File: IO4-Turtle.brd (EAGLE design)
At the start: 50 x 68.6 mm, 30 parts, among them CON1 RJ12/6, IC1 TC4428A, IC2 NE555S, Q1 NPN, X2 MSTBA5

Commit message: added values for connectors
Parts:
- J1: value (none) -> 0.156
- LMP1: value (none) -> 12v

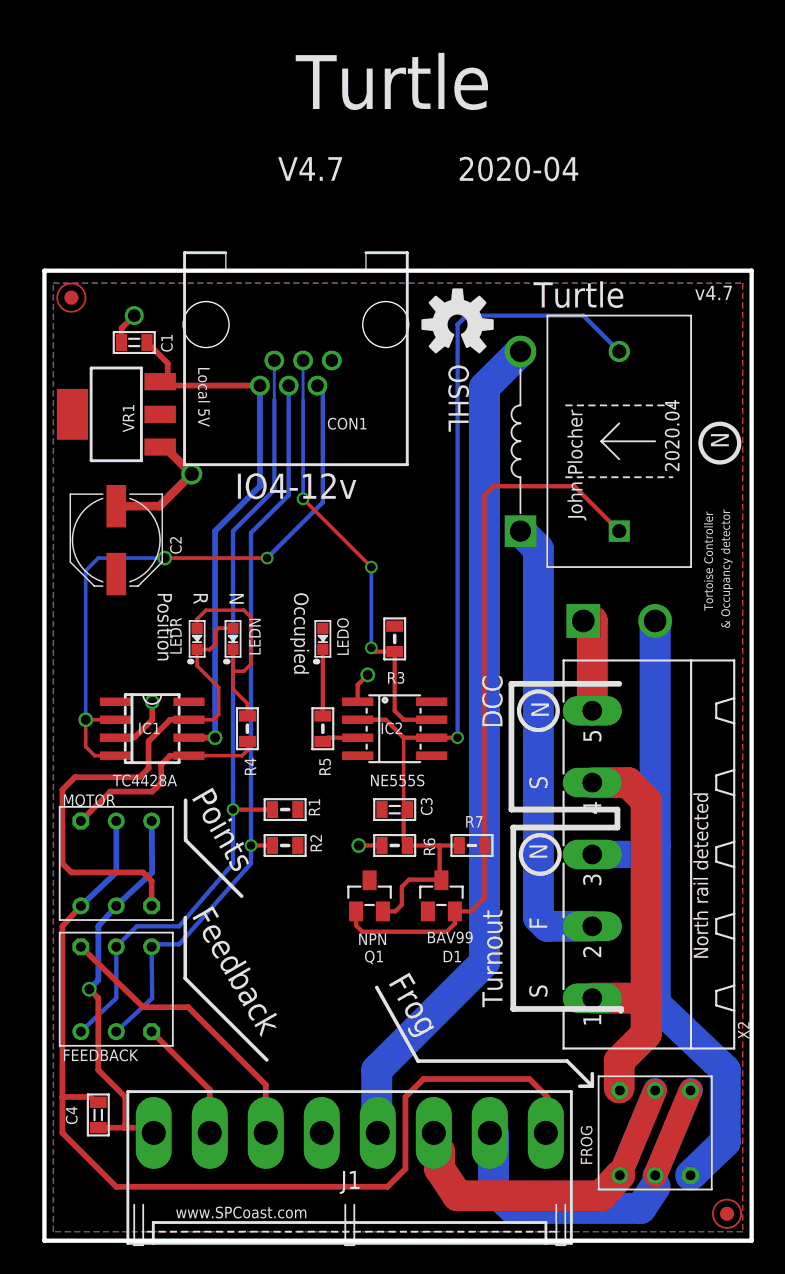
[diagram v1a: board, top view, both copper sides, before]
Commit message: added values for connectors
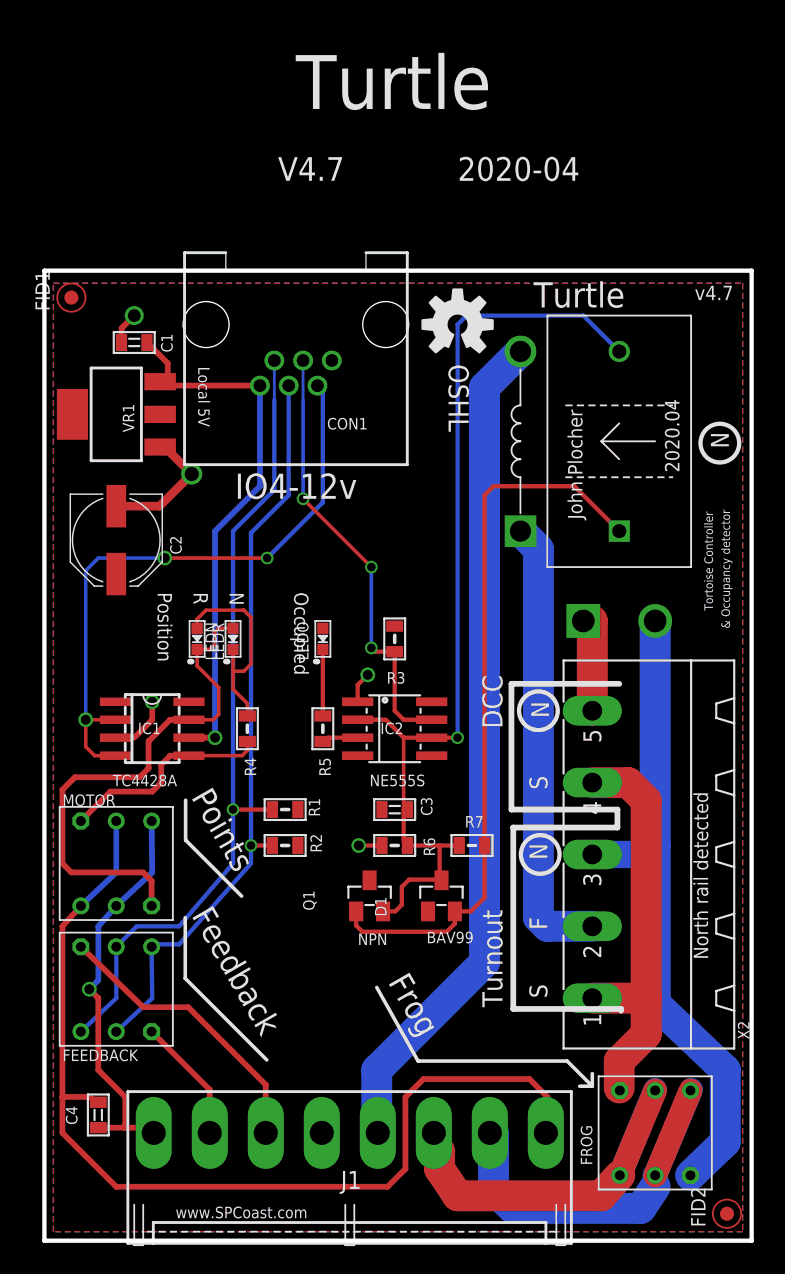
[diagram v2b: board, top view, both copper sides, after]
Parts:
- turned D1 to 270 degrees
- turned Q1 to 270 degrees
- turned LEDN to 90 degrees
- turned LEDO to 90 degrees
- turned LEDR to 90 degrees
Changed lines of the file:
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@@
 <setting verticaltext="up"/>
 </settings>
-<grid distance="50" unitdist="mil" unit="mil" style="dots" multiple="2" display="yes" altdistance="25" altunitdist="mil" altunit="mil"/>
+<grid distance="50" unitdist="mil" unit="mm" style="dots" multiple="2" display="yes" altdistance="25" altunitdist="mil" altunit="mil"/>
 <layers>
 <layer number="1" name="Top" color="4" fill="1" visible="yes" active="yes"/>
@@
 <layer number="123" name="tTestmark" color="7" fill="1" visible="no" active="yes"/>
 <layer number="124" name="bTestmark" color="7" fill="1" visible="no" active="yes"/>
-<layer number="125" name="_tNames" color="14" fill="1" visible="no" active="no"/>
+<layer number="125" name="_tNames" color="14" fill="1" visible="no" active="yes"/>
 <layer number="126" name="_bNames" color="7" fill="1" visible="no" active="yes"/>
 <layer number="127" name="_tValues" color="7" fill="1" visible="no" active="no"/>
@@
 <text x="49.8475" y="14.224" size="0.8128" layer="125" font="vector" ratio="10" rot="R90">X2</text>
 <wire x1="26.416" y1="12.7" x2="23.495" y2="17.907" width="0.254" layer="21"/>
+<text x="8.255" y="64.135" size="0.8128" layer="125" font="vector" rot="R270">C1</text>
+<text x="8.89" y="49.8475" size="0.8128" layer="125" font="vector" rot="R270">C2</text>
+<text x="27.432" y="30.0355" size="0.8128" layer="125" font="vector" rot="R90">C3</text>
+<text x="1.524" y="9.525" size="0.8128" layer="125" font="vector" rot="R270">C4</text>
+<text x="22.86" y="58.166" size="0.8128" layer="125" font="vector" rot="R180">CON1</text>
+<text x="28.1305" y="19.685" size="0.8128" layer="125" font="vector">D1</text>
+<text x="1.27" y="12.7" size="0.8128" layer="125" font="vector">FEEDBACK</text>
+<text x="38.735" y="5.334" size="0.8128" layer="125" font="vector" rot="R90">FROG</text>
+<text x="6.604" y="35.814" size="0.8128" layer="125" font="vector">IC1</text>
+<text x="23.749" y="35.814" size="0.8128" layer="125" font="vector">IC2</text>
+<text x="20.955" y="3.6599875" size="1.27" layer="125" font="vector">J1</text>
+<text x="14.478" y="44.069" size="0.8128" layer="125" font="vector" rot="R270">LEDN</text>
+<text x="20.701" y="44.069" size="0.8128" layer="125" font="vector" rot="R270">LEDO</text>
+<text x="8.89" y="44.069" size="0.8128" layer="125" font="vector" rot="R270">LEDR</text>
+<text x="1.27" y="30.734" size="0.8128" layer="125" font="vector">MOTOR</text>
+<text x="22.606" y="19.685" size="0.8128" layer="125" font="vector">Q1</text>
+<text x="19.4945" y="29.972" size="0.8128" layer="125" font="vector" rot="R90">R1</text>
+<text x="19.6215" y="27.432" size="0.8128" layer="125" font="vector" rot="R90">R2</text>
+<text x="25.527" y="40.1955" size="0.8128" layer="125" font="vector" rot="R180">R3</text>
+<text x="14.1605" y="34.163" size="0.8128" layer="125" font="vector" rot="R270">R4</text>
+<text x="19.431" y="34.163" size="0.8128" layer="125" font="vector" rot="R270">R5</text>
+<text x="27.6225" y="27.178" size="0.8128" layer="125" font="vector" rot="R90">R6</text>
+<text x="29.718" y="29.21" size="0.8128" layer="125" font="vector">R7</text>
+<text x="6.35" y="57.15" size="0.8128" layer="125" font="vector" rot="R90">VR1</text>
+<text x="49.8475" y="14.224" size="0.8128" layer="125" font="vector" ratio="10" rot="R90">X2</text>
 </plain>
 <attributes>
@@
 <attribute name="VALUE" x="1.6002" y="48.514" size="0.8128" layer="27" font="vector" rot="R90"/>
 </element>
-<element name="LEDO" library="SPCoast" package="0603-LED" value="Y" x="19.685" y="42.545" smashed="yes" rot="R270">
-<attribute name="NAME" x="20.701" y="44.069" size="0.8128" layer="25" rot="R270"/>
-<attribute name="VALUE" x="19.939" y="39.751" size="0.8128" layer="27" font="vector" rot="R90"/>
+<element name="LEDO" library="SPCoast" package="0603-LED" value="Y" x="19.685" y="42.545" smashed="yes" rot="R90">
+<attribute name="NAME" x="18.669" y="41.021" size="0.8128" layer="25" rot="R90"/>
+<attribute name="VALUE" x="19.431" y="45.339" size="0.8128" layer="27" font="vector" rot="R270"/>
 </element>
 <element name="X2" library="SPCoast" package="MSTBA5" value="MSTBA5" x="43.815" y="27.305" smashed="yes" rot="R90">
@@
 <attribute name="OC_NEWARK" value="71C4164" x="43.815" y="27.305" size="1.778" layer="27" rot="R90" display="off"/>
 </element>
-<element name="LEDR" library="SPCoast" package="0603-LED" value="R" x="10.795" y="42.545" smashed="yes" rot="R270">
-<attribute name="NAME" x="8.89" y="44.069" size="0.8128" layer="25" rot="R270"/>
-<attribute name="VALUE" x="11.049" y="39.751" size="0.8128" layer="27" font="vector" rot="R90"/>
-</element>
-<element name="LEDN" library="SPCoast" package="0603-LED" value="G" x="13.335" y="42.545" smashed="yes" rot="R270">
-<attribute name="NAME" x="14.478" y="44.069" size="0.8128" layer="25" rot="R270"/>
-<attribute name="VALUE" x="13.589" y="39.751" size="0.8128" layer="27" font="vector" rot="R90"/>
-</element>
-<element name="D1" library="SPCoast" package="SOT23" value="BAV99" x="28.067" y="24.384" smashed="yes">
-<attribute name="NAME" x="28.1305" y="19.685" size="0.8128" layer="25"/>
-<attribute name="VALUE" x="30.353" y="21.844" size="0.8128" layer="27" font="vector" rot="R180"/>
-</element>
-<element name="Q1" library="SPCoast" package="SOT23" value="NPN" x="22.987" y="24.384" smashed="yes">
-<attribute name="NAME" x="22.606" y="19.685" size="0.8128" layer="25"/>
-<attribute name="VALUE" x="24.257" y="21.717" size="0.8128" layer="27" font="vector" rot="R180"/>
+<element name="LEDR" library="SPCoast" package="0603-LED" value="R" x="10.795" y="42.545" smashed="yes" rot="R90">
+<attribute name="NAME" x="12.7" y="41.021" size="0.8128" layer="25" rot="R90"/>
+<attribute name="VALUE" x="10.541" y="45.339" size="0.8128" layer="27" font="vector" rot="R270"/>
+</element>
+<element name="LEDN" library="SPCoast" package="0603-LED" value="G" x="13.335" y="42.545" smashed="yes" rot="R90">
+<attribute name="NAME" x="12.192" y="41.021" size="0.8128" layer="25" rot="R90"/>
+<attribute name="VALUE" x="13.081" y="45.339" size="0.8128" layer="27" font="vector" rot="R270"/>
+</element>
+<element name="D1" library="SPCoast" package="SOT23" value="BAV99" x="28.07" y="24.38" smashed="yes" rot="R270">
+<attribute name="NAME" x="23.371" y="24.3165" size="0.8128" layer="25" rot="R270"/>
+<attribute name="VALUE" x="25.53" y="22.094" size="0.8128" layer="27" font="vector" rot="R90"/>
+</element>
+<element name="Q1" library="SPCoast" package="SOT23" value="NPN" x="22.99" y="24.38" smashed="yes" rot="R270">
+<attribute name="NAME" x="18.291" y="24.761" size="0.8128" layer="25" rot="R270"/>
+<attribute name="VALUE" x="20.323" y="23.11" size="0.8128" layer="27" font="vector" rot="R90"/>
 </element>
 <element name="IC2" library="SPCoast" package="SO08" value="NE555S" x="24.765" y="36.195" smashed="yes" rot="R270">
@@
 <wire x1="31.115" y1="27.94" x2="31.115" y2="24.257" width="0.3048" layer="1"/>
 <wire x1="31.115" y1="24.257" x2="30.142" y2="23.284" width="0.3048" layer="1"/>
-<wire x1="30.142" y1="23.284" x2="29.017" y2="23.284" width="0.3048" layer="1"/>
-<wire x1="22.037" y1="23.284" x2="22.037" y2="22.286" width="0.3048" layer="1"/>
+<wire x1="30.142" y1="23.284" x2="29.02" y2="23.28" width="0.3048" layer="1"/>
+<wire x1="22.04" y1="23.28" x2="22.037" y2="22.286" width="0.3048" layer="1"/>
 <wire x1="22.037" y1="22.286" x2="22.479" y2="21.844" width="0.3048" layer="1"/>
 <wire x1="22.479" y1="21.844" x2="28.448" y2="21.844" width="0.3048" layer="1"/>
 <wire x1="28.448" y1="21.844" x2="29.017" y2="22.413" width="0.3048" layer="1"/>
-<wire x1="29.017" y1="22.413" x2="29.017" y2="23.284" width="0.3048" layer="1"/>
+<wire x1="29.017" y1="22.413" x2="29.02" y2="23.28" width="0.3048" layer="1"/>
 </signal>
 <signal name="TRIGGER">
@@
 <wire x1="27.94" y1="27.94" x2="25.665" y2="27.94" width="0.3048" layer="1"/>
 <wire x1="25.4" y1="27.675" x2="25.665" y2="27.94" width="0.3048" layer="1"/>
-<wire x1="23.937" y1="23.284" x2="24.808" y2="23.284" width="0.3048" layer="1"/>
+<wire x1="23.94" y1="23.28" x2="24.808" y2="23.284" width="0.3048" layer="1"/>
 <wire x1="24.808" y1="23.284" x2="25.273" y2="23.749" width="0.3048" layer="1"/>
 <wire x1="25.273" y1="23.749" x2="25.273" y2="25.019" width="0.3048" layer="1"/>
 <wire x1="25.273" y1="25.019" x2="25.781" y2="25.527" width="0.3048" layer="1"/>
 <wire x1="25.781" y1="25.527" x2="28.024" y2="25.527" width="0.3048" layer="1"/>
-<wire x1="28.024" y1="25.527" x2="28.067" y2="25.484" width="0.3048" layer="1"/>
-<wire x1="28.067" y1="25.484" x2="27.94" y2="25.611" width="0.3048" layer="1"/>
+<wire x1="28.024" y1="25.527" x2="28.07" y2="25.48" width="0.3048" layer="1"/>
+<wire x1="28.07" y1="25.48" x2="27.94" y2="25.611" width="0.3048" layer="1"/>
 <wire x1="27.94" y1="25.611" x2="27.94" y2="27.94" width="0.3048" layer="1"/>
 <wire x1="27.3812" y1="35.56" x2="29.21" y2="35.56" width="0.3048" layer="1"/>

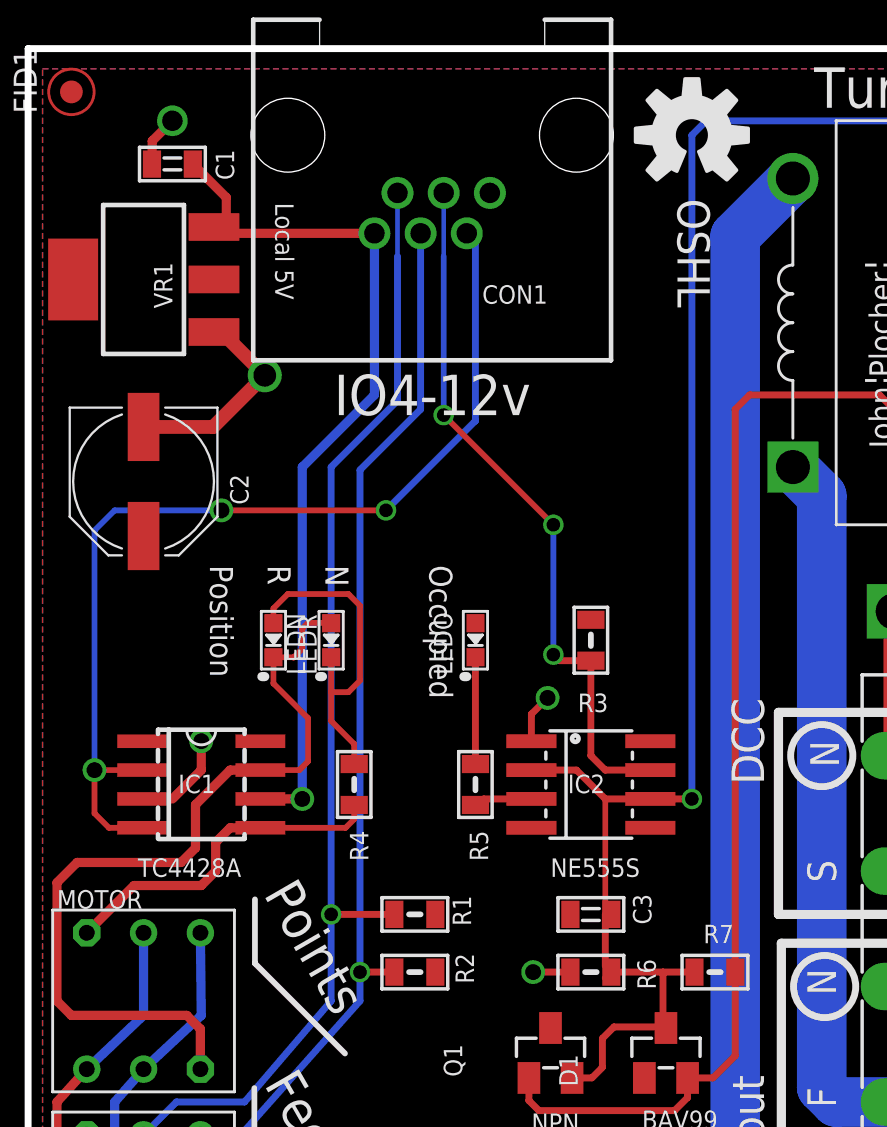
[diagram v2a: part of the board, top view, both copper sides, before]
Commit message: normalized values
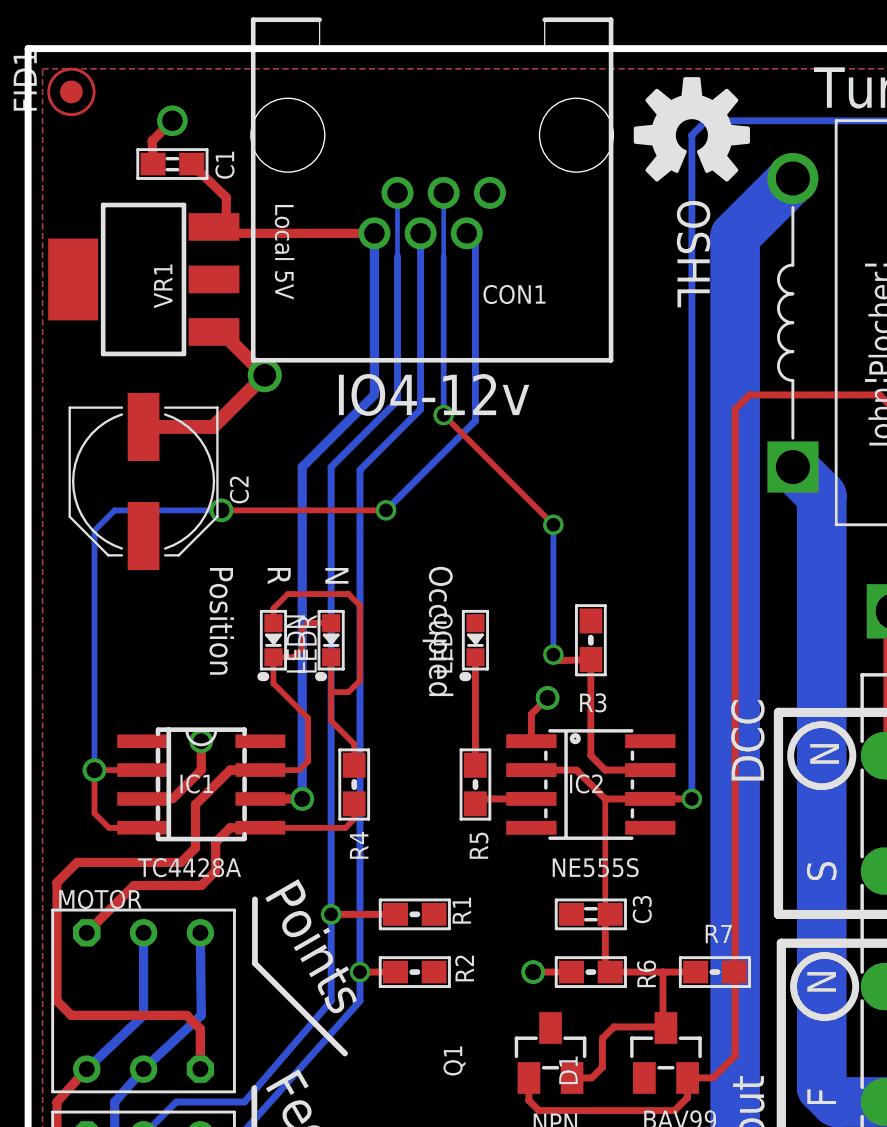
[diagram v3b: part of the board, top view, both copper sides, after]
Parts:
- C1, C3: device SPCoast:0805-CAP -> SPCoast:0603-CAP
- OSHW1: value DOC-OSHW-LOGO-M -> OSHW
- R1, R2, R3, R4, R5, R6, R7: device SPCoast:0805-RES -> SPCoast:0603-RES
- X2: value MSTBA5 -> 0.200
